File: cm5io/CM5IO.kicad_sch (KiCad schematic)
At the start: 12 parts, among them J11 USB_C_Receptacle_USB2.0

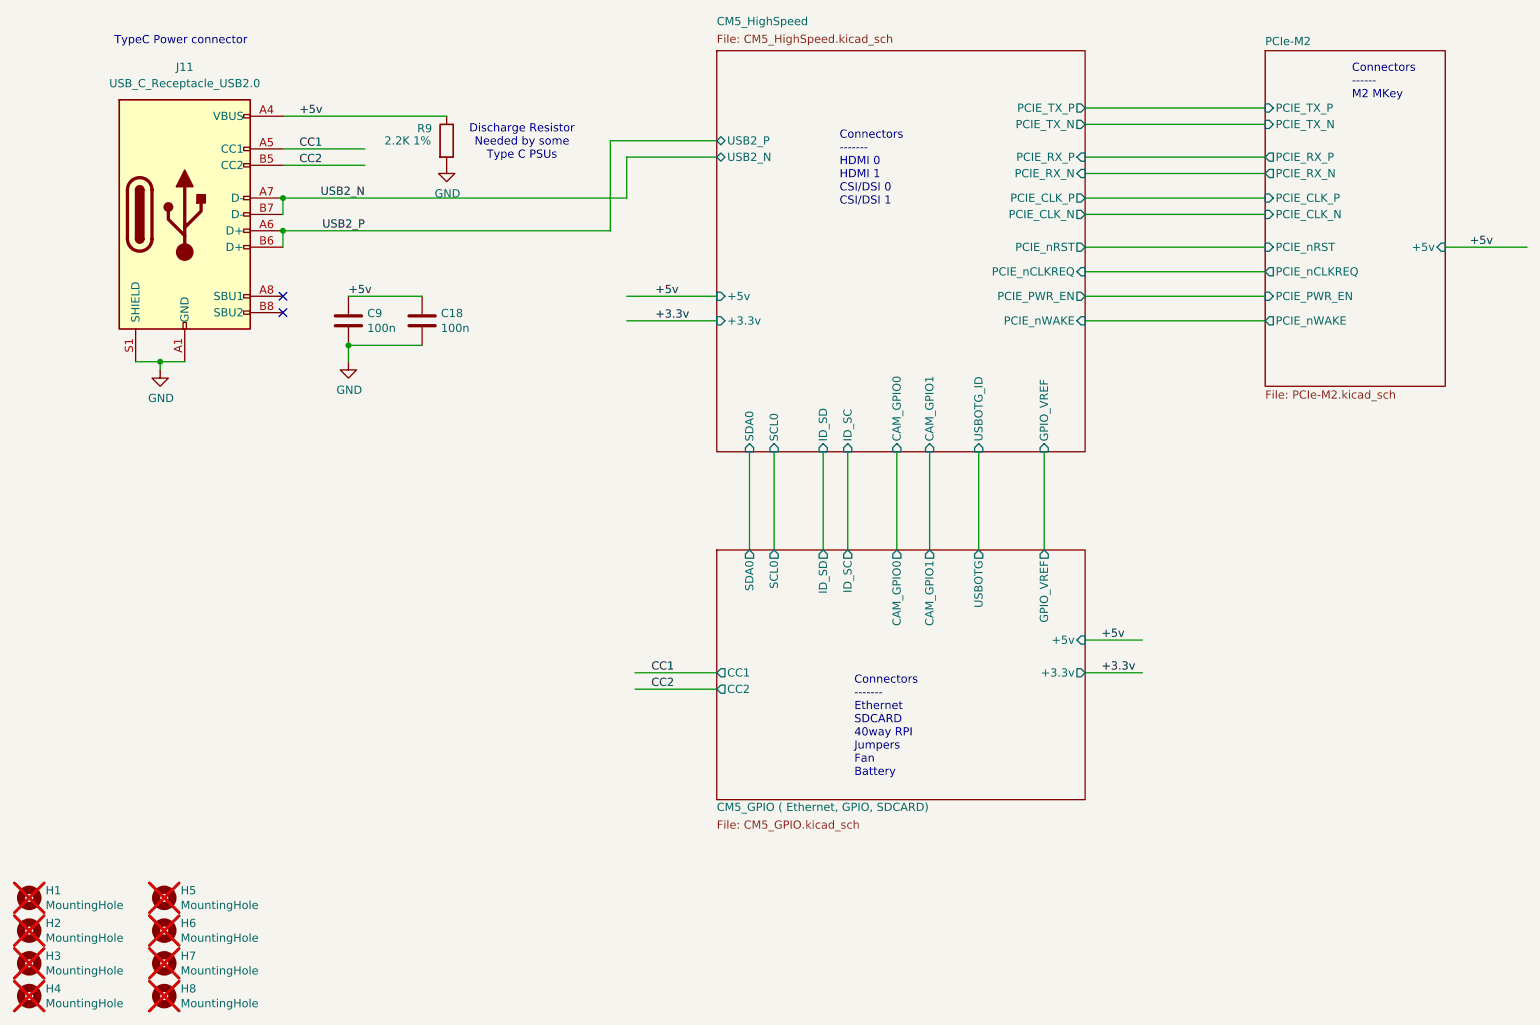
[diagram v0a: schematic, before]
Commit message: [cm5io] remove USB-C and NVMe connectors, clean up routing
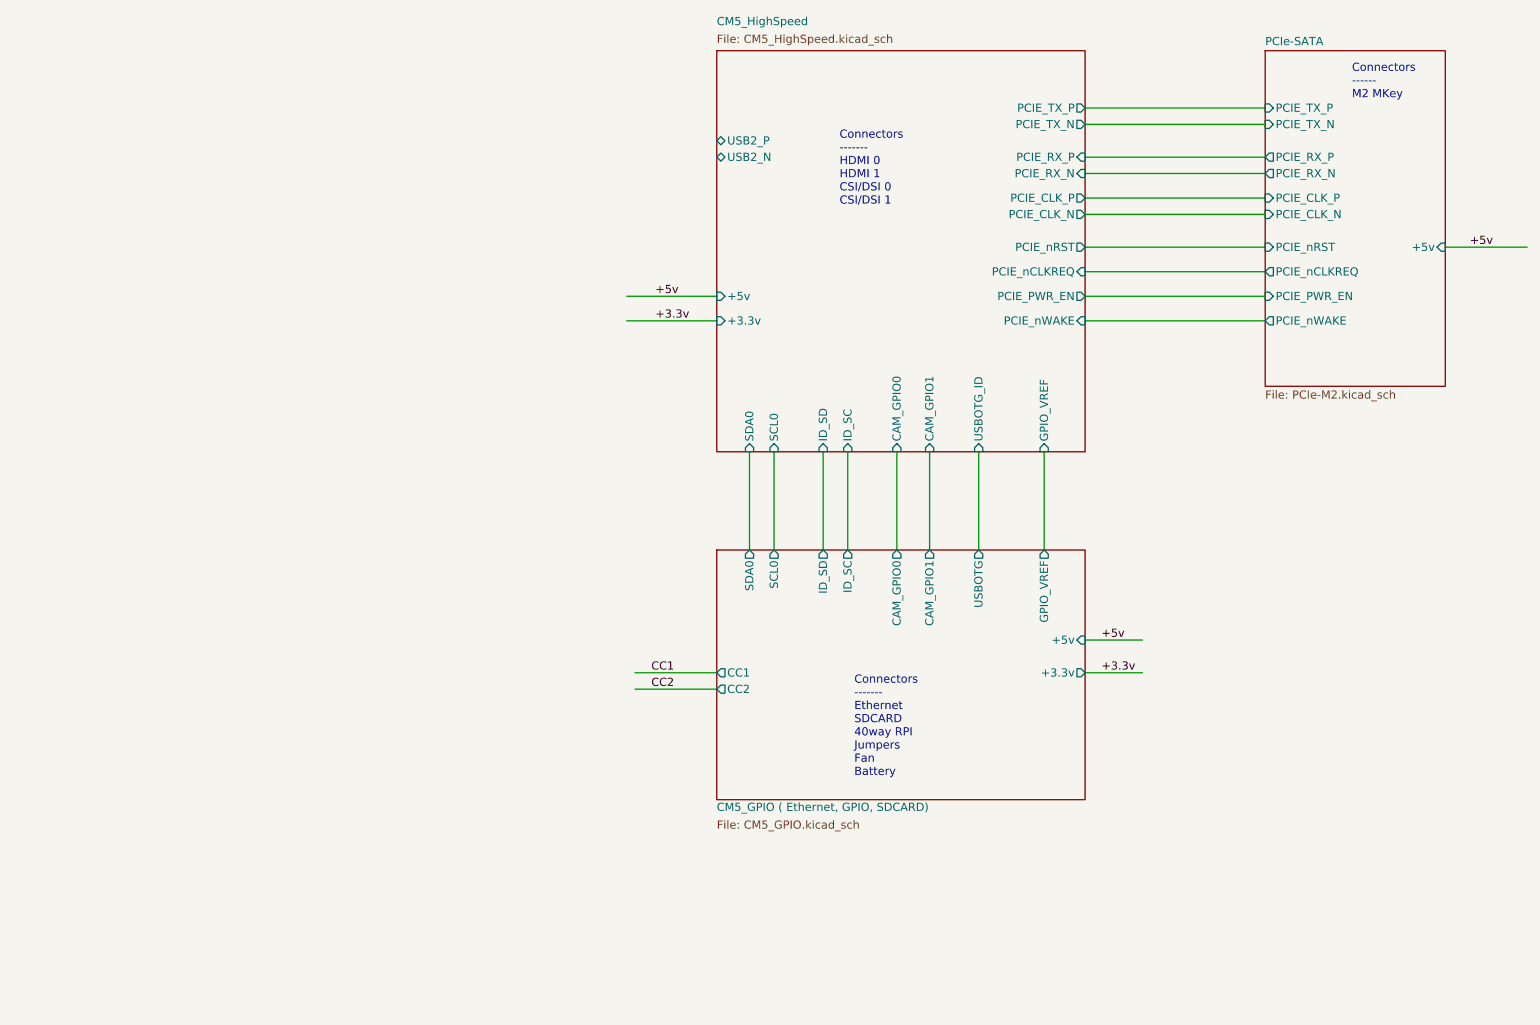
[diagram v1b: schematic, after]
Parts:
- removed C18, C9: 100n, Capacitor_SMD:C_0402_1005Metric, symbol Device:C
- removed H1, H2, H3, H4, H5, H6, H7, H8: MountingHole, CM5IO:MountingHole_2.7mm_M2.5_DIN965, symbol Mechanical:MountingHole
- removed J11: USB_C_Receptacle_USB2.0, Connector_USB:USB_C_Receptacle_GCT_USB4105-xx-A_16P_TopMnt_Horizontal, symbol Connector:USB_C_Receptacle_USB2.0_16P
- removed R9: 2.2K 1%, Resistor_SMD:R_0402_1005Metric, symbol Device:R
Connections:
- no-connect marks 2 -> 0
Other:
- sheet PCIe-M2 renamed PCIe-SATA
- note removed: "Discharge Resistor Needed by some Type C PSUs"
- note removed: "TypeC Power connector"
